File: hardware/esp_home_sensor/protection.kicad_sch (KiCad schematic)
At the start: 9 parts

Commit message: busses, display connector, footprint lib
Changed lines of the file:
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@@
 		(lib_id "Device:C")
 		(at 109.22 106.68 0)
+		(mirror y)
 		(unit 1)
 		(body_style 1)
@@
 		(in_pos_files yes)
 		(dnp no)
-		(fields_autoplaced yes)
 		(property "Reference" "C3"
-			(at 113.03 105.4099 0)
+			(at 105.41 105.4099 0)
 			(show_name no)
 			(do_not_autoplace no)
@@
 		)
 		(property "Value" "C"
-			(at 113.03 107.9499 0)
+			(at 105.41 107.9499 0)
 			(show_name no)
 			(do_not_autoplace no)
@@
 		)
 		(property "Footprint" ""
-			(at 110.1852 110.49 0)
+			(at 108.2548 110.49 0)
 			(hide yes)
 			(show_name no)

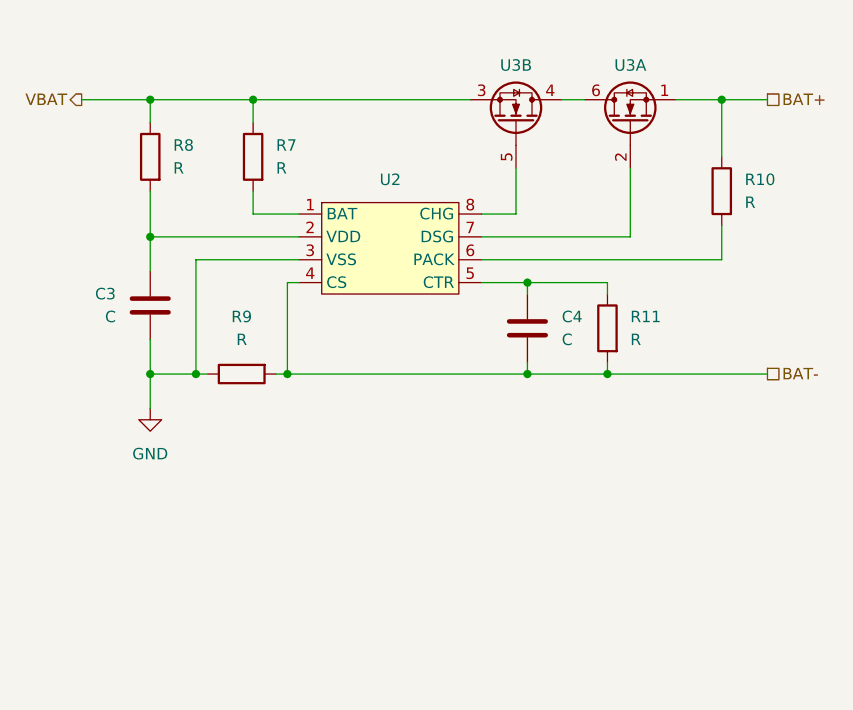
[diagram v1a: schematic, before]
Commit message: footprint assignment, buck
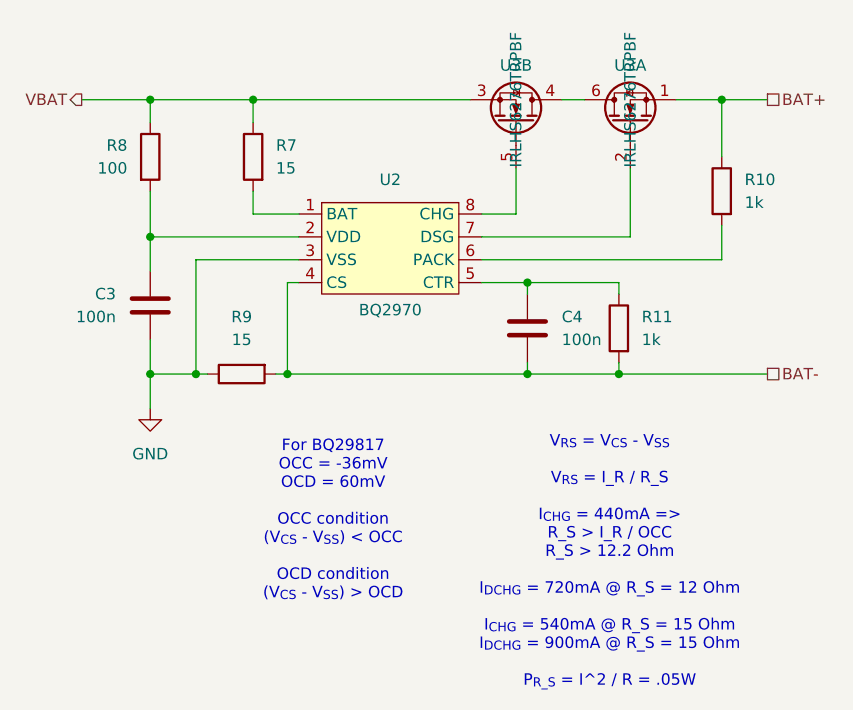
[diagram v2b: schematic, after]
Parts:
- C3, C4: value C -> 100n; footprint (none) -> Capacitor_SMD:C_0402_1005Metric
- R10, R11: value R -> 1k; footprint (none) -> Resistor_SMD:R_0402_1005Metric
- R7, R9: value R -> 15; footprint (none) -> Resistor_SMD:R_0402_1005Metric
- R8: value R -> 100; footprint (none) -> Resistor_SMD:R_0402_1005Metric
- U2: value (none) -> BQ2970; footprint (none) -> esp_home_sensor:QFN-8_1.5x1.5_Pitch0.5mm; Mfr. No. (none) -> BQ298217RUGR
- U3: value (none) -> IRLHS6276TRPBF; footprint (none) -> esp_home_sensor:QFN-6_2x2_Pitch0.65mm; Mfr. No. (none) -> IRLHS6276TRPBF
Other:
- note added: "For BQ29817 OCC = -36mV OCD = 60mV OCC condition (V_{CS} - V_{SS}) < OCC OCD condition (V_{CS} - V_{SS}) > OCD"
- note added: "V_{RS} = V_{CS} - V_{SS} V_{RS} = I_R / R_S I_{CHG} = 440mA => R_S > I_R / OCC R_S > 12.2 Ohm I_{DCHG} = 720mA @ R_S = 12 Ohm I_{CHG} = 540mA @ R_S = 15 Ohm I_{DCHG} = 900mA @ R_S = 15 Ohm P_{R_S} = I^2 / R = .05W"
- moved on the sheet: R11

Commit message: initial layout, power routing
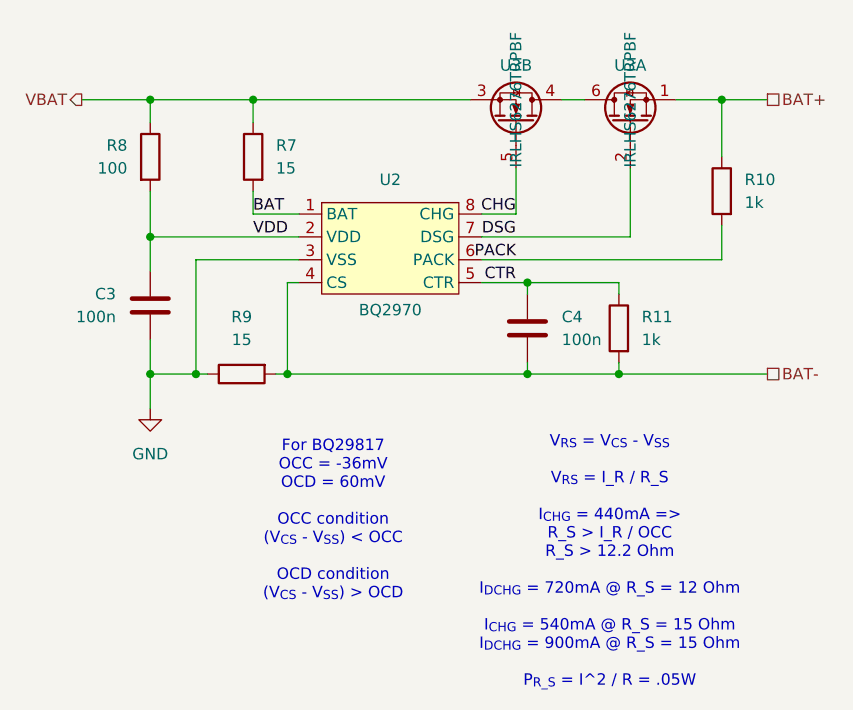
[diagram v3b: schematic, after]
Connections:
- net BAT: now reaches R7.2, U2.1 (BAT)
- net DSG: now reaches U2.7 (DSG), U3.2
- net CTR: now reaches C4.1, R11.1, U2.5 (CTR)
- net VDD: now reaches C3.1, R8.2, U2.2 (VDD)
- net PACK: now reaches R10.2, U2.6 (PACK)
- net CHG: now reaches U2.8 (CHG), U3.5
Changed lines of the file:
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@@
+		)
+	)
+	(label "VDD"
+		(at 120.65 99.06 0)
+		(effects
+			(font
+				(size 1.27 1.27)
+			)
+			(justify left bottom)
+		)
+	)
+	(label "BAT"
+		(at 120.65 96.52 0)
+		(effects
+			(font
+				(size 1.27 1.27)
+			)
+			(justify left bottom)
+		)
+	)
+	(label "CHG"
+		(at 149.86 96.52 180)
+		(effects
+			(font
+				(size 1.27 1.27)
+			)
+			(justify right bottom)
+		)
+	)
+	(label "PACK"
+		(at 149.86 101.6 180)
+		(effects
+			(font
+				(size 1.27 1.27)
+			)
+			(justify right bottom)
+		)
+	)
+	(label "DSG"
+		(at 149.86 99.06 180)
+		(effects
+			(font
+				(size 1.27 1.27)
+			)
+			(justify right bottom)
+		)
+	)
+	(label "CTR"
+		(at 149.86 104.14 180)
+		(effects
+			(font
+				(size 1.27 1.27)
+			)
+			(justify right bottom)
 		)
 	)
@@
 		)
 	)
+	(netclass_flag ""
+		(length 2.54)
+		(shape round)
+		(at 172.72 114.3 0)
+		(fields_autoplaced yes)
+		(effects
+			(font
+				(size 1.27 1.27)
+			)
+			(justify left bottom)
+		)
+		(property "Klasy sieci" "Power"
+			(at 173.4185 111.76 0)
+			(show_name no)
+			(do_not_autoplace no)
+			(effects
+				(font
+					(size 1.27 1.27)
+				)
+				(justify left)
+			)
+		)
+		(property "Component Class" ""
+			(at 73.66 45.72 0)
+			(show_name no)
+			(do_not_autoplace no)
+			(effects
+				(font
+					(size 1.27 1.27)
+					(italic yes)
+				)
+			)
+		)
+	)
+	(netclass_flag ""
+		(length 2.54)
+		(shape round)
+		(at 172.72 83.82 0)
+		(fields_autoplaced yes)
+		(effects
+			(font
+				(size 1.27 1.27)
+			)
+			(justify left bottom)
+		)
+		(property "Klasy sieci" "Power"
+			(at 173.4185 81.28 0)
+			(show_name no)
+			(do_not_autoplace no)
+			(effects
+				(font
+					(size 1.27 1.27)
+				)
+				(justify left)
+			)
+		)
+		(property "Component Class" ""
+			(at 73.66 15.24 0)
+			(show_name no)
+			(do_not_autoplace no)
+			(effects
+				(font
+					(size 1.27 1.27)
+					(italic yes)
+				)
+			)
+		)
+	)

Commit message: layout
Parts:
- renumbered R7 to R10, R10 to R12
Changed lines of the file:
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@@
 		(dnp no)
 		(fields_autoplaced yes)
-		(property "Reference" "R7"
+		(property "Reference" "R10"
 			(at 123.19 88.8999 0)
 			(show_name no)
@@
 			(project "esp_home_sensor"
 				(path "/1b1bee14-8d82-405b-b99d-415549a137e6/b8302090-6617-4f26-9a2f-2058e60ddfbb"
-					(reference "R7")
+					(reference "R10")
 					(unit 1)
 				)
@@
 		(in_pos_files yes)
 		(dnp no)
-		(property "Reference" "#PWR08"
+		(property "Reference" "#PWR024"
 			(at 109.22 124.46 0)
 			(hide yes)
@@
 			(project "esp_home_sensor"
 				(path "/1b1bee14-8d82-405b-b99d-415549a137e6/b8302090-6617-4f26-9a2f-2058e60ddfbb"
-					(reference "#PWR08")
+					(reference "#PWR024")
 					(unit 1)
 				)
@@
 		(dnp no)
 		(fields_autoplaced yes)
-		(property "Reference" "R10"
+		(property "Reference" "R12"
 			(at 175.26 92.7099 0)
 			(show_name no)
@@
 			(project "esp_home_sensor"
 				(path "/1b1bee14-8d82-405b-b99d-415549a137e6/b8302090-6617-4f26-9a2f-2058e60ddfbb"
-					(reference "R10")
+					(reference "R12")
 					(unit 1)
 				)

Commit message: in production
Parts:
- C3, C4: Mfr. No. (none) -> GRM155R71H104KE14D
- R10, R9: Mfr. No. (none) -> AC0402FR-7W15RL
- R11, R12: Mfr. No. (none) -> RC0402JR-7W1KL
- R8: Mfr. No. (none) -> RT0402DRE07100RL
- U2: Mfr. No. BQ298217RUGR -> BQ298217RUGR
- U3: Mfr. No. IRLHS6276TRPBF -> IRLHS6276TRPBF
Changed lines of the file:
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@@
 			)
 		)
-		(property "Mfr. No." ""
+		(property "Mfr. No." "AC0402FR-7W15RL"
 			(at 120.65 90.17 0)
 			(hide yes)
@@
 			)
 		)
-		(property "Mfr. No." "IRLHS6276TRPBF "
+		(property "Mfr. No." "IRLHS6276TRPBF"
 			(at 162.56 83.82 90)
 			(hide yes)
@@
 			)
 		)
-		(property "Mfr. No." ""
+		(property "Mfr. No." "AC0402FR-7W15RL"
 			(at 119.38 114.3 90)
 			(hide yes)
@@
 			)
 		)
-		(property "Mfr. No." ""
+		(property "Mfr. No." "GRM155R71H104KE14D"
 			(at 151.13 109.22 0)
 			(hide yes)
@@
 			)
 		)
-		(property "Mfr. No." "BQ298217RUGR "
+		(property "Mfr. No." "BQ298217RUGR"
 			(at 135.89 100.33 0)
 			(hide yes)
@@
 			)
 		)
-		(property "Mfr. No." "IRLHS6276TRPBF "
+		(property "Mfr. No." "IRLHS6276TRPBF"
 			(at 149.86 83.82 90)
 			(hide yes)
@@
 			)
 		)
-		(property "Mfr. No." ""
+		(property "Mfr. No." "RT0402DRE07100RL"
 			(at 109.22 90.17 0)
 			(hide yes)
@@
 			)
 		)
-		(property "Mfr. No." ""
+		(property "Mfr. No." "RC0402JR-7W1KL"
 			(at 172.72 93.98 0)
 			(hide yes)
@@
 			)
 		)
-		(property "Mfr. No." ""
+		(property "Mfr. No." "GRM155R71H104KE14D"
 			(at 109.22 106.68 0)
 			(hide yes)
@@
 			)
 		)
-		(property "Mfr. No." ""
+		(property "Mfr. No." "RC0402JR-7W1KL"
 			(at 161.29 109.22 0)
 			(hide yes)

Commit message: az
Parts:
- U2: Down_current (none) -> 100n; Supply_current (none) -> 4u
- U3: Down_current (none) -> 100n; Supply_current (none) -> N/A
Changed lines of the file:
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@@
+			)
+		)
+		(property "Down_current" ""
+			(at 120.65 90.17 0)
+			(hide yes)
+			(show_name no)
+			(do_not_autoplace no)
+			(effects
+				(font
+					(size 1.27 1.27)
+				)
+			)
+		)
+		(property "Supply_current" ""
+			(at 120.65 90.17 0)
+			(hide yes)
+			(show_name no)
+			(do_not_autoplace no)
+			(effects
+				(font
+					(size 1.27 1.27)
+				)
 			)
 		)
@@
 		)
 		(property "Mfr. No." "IRLHS6276TRPBF"
+			(at 162.56 83.82 90)
+			(hide yes)
+			(show_name no)
+			(do_not_autoplace no)
+			(effects
+				(font
+					(size 1.27 1.27)
+				)
+			)
+		)
+		(property "Down_current" "100n"
+			(at 162.56 83.82 90)
+			(hide yes)
+			(show_name no)
+			(do_not_autoplace no)
+			(effects
+				(font
+					(size 1.27 1.27)
+				)
+			)
+		)
+		(property "Supply_current" "N/A"
 			(at 162.56 83.82 90)
 			(hide yes)
@@
 			)
 		)
+		(property "Down_current" ""
+			(at 119.38 114.3 90)
+			(hide yes)
+			(show_name no)
+			(do_not_autoplace no)
+			(effects
+				(font
+					(size 1.27 1.27)
+				)
+			)
+		)
+		(property "Supply_current" ""
+			(at 119.38 114.3 90)
+			(hide yes)
+			(show_name no)
+			(do_not_autoplace no)
+			(effects
+				(font
+					(size 1.27 1.27)
+				)
+			)
+		)
 		(pin "1"
 		)
@@
 			)
 		)
+		(property "Down_current" ""
+			(at 151.13 109.22 0)
+			(hide yes)
+			(show_name no)
+			(do_not_autoplace no)
+			(effects
+				(font
+					(size 1.27 1.27)
+				)
+			)
+		)
+		(property "Supply_current" ""
+			(at 151.13 109.22 0)
+			(hide yes)
+			(show_name no)
+			(do_not_autoplace no)
+			(effects
+				(font
+					(size 1.27 1.27)
+				)
+			)
+		)
 		(pin "2"
 		)
@@
 		)
 		(property "Mfr. No." "BQ298217RUGR"
+			(at 135.89 100.33 0)
+			(hide yes)
+			(show_name no)
+			(do_not_autoplace no)
+			(effects
+				(font
+					(size 1.27 1.27)
+				)
+			)
+		)
+		(property "Down_current" "100n"
+			(at 135.89 100.33 0)
+			(hide yes)
+			(show_name no)
+			(do_not_autoplace no)
+			(effects
+				(font
+					(size 1.27 1.27)
+				)
+			)
+		)
+		(property "Supply_current" "4u"
 			(at 135.89 100.33 0)
 			(hide yes)
@@
 			)
 		)
+		(property "Down_current" "100n"
+			(at 149.86 83.82 90)
+			(hide yes)
+			(show_name no)
+			(do_not_autoplace no)
+			(effects
+				(font
+					(size 1.27 1.27)
+				)
+			)
+		)
+		(property "Supply_current" "N/A"
+			(at 149.86 83.82 90)
+			(hide yes)
+			(show_name no)
+			(do_not_autoplace no)
+			(effects
+				(font
+					(size 1.27 1.27)
+				)
+			)
+		)
 		(pin "6"
 		)
@@
 		)
 		(property "Mfr. No." "RT0402DRE07100RL"
+			(at 109.22 90.17 0)
+			(hide yes)
+			(show_name no)
+			(do_not_autoplace no)
+			(effects
+				(font
+					(size 1.27 1.27)
+				)
+			)
+		)
+		(property "Down_current" ""
+			(at 109.22 90.17 0)
+			(hide yes)
+			(show_name no)
+			(do_not_autoplace no)
+			(effects
+				(font
+					(size 1.27 1.27)
+				)
+			)
+		)
+		(property "Supply_current" ""
 			(at 109.22 90.17 0)
 			(hide yes)
@@
 			)
 		)
+		(property "Down_current" ""
+			(at 172.72 93.98 0)
+			(hide yes)
+			(show_name no)
+			(do_not_autoplace no)
+			(effects
+				(font
+					(size 1.27 1.27)
+				)
+			)
+		)
+		(property "Supply_current" ""
+			(at 172.72 93.98 0)
+			(hide yes)
+			(show_name no)
+			(do_not_autoplace no)
+			(effects
+				(font
+					(size 1.27 1.27)
+				)
+			)
+		)
 		(pin "1"
 		)
@@
 		)
 		(property "Mfr. No." "GRM155R71H104KE14D"
+			(at 109.22 106.68 0)
+			(hide yes)
+			(show_name no)
+			(do_not_autoplace no)
+			(effects
+				(font
+					(size 1.27 1.27)
+				)
+			)
+		)
+		(property "Down_current" ""
+			(at 109.22 106.68 0)
+			(hide yes)
+			(show_name no)
+			(do_not_autoplace no)
+			(effects
+				(font
+					(size 1.27 1.27)
+				)
+			)
+		)
+		(property "Supply_current" ""
 			(at 109.22 106.68 0)
 			(hide yes)
@@
 			(at 161.29 109.22 0)
 			(hide yes)
+			(show_name no)
+			(do_not_autoplace no)
+			(effects
+				(font
+					(size 1.27 1.27)
+				)
+			)
+		)
+		(property "Down_current" ""
+			(at 161.29 109.22 0)
+			(hide yes)
+			(show_name no)
+			(do_not_autoplace no)
+			(effects
+				(font
+					(size 1.27 1.27)
+				)
+			)
+		)
+		(property "Supply_current" ""
+			(at 161.29 109.22 0)
+			(hide yes)
